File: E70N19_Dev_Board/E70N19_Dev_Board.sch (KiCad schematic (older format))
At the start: 71 parts, among them J1 USB_OTG, J2 Battery 1x2, J3 JTAGSEL_JUMPER 1x3, J4 UART_PROG 1x2, J5 ERASE_JUMPER 1x3, J6 ARM-Cortex-Debug-10, J7 CAN 1x2, J8 Conn_02x15_Counter_Clockwise, J9 Conn_02x15_Counter_Clockwise, SW1 NRST_BUTTON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

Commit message: Brad's micro OTG connector
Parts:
- removed J1: USB_OTG, Connect:USB_Micro-B, symbol USB_OTG-RESCUE-E70N19_Dev_Board
- added J?: USB_microB_2040002-1, symbol USB_microB_2040002-1
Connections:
- wire segments 231 -> 238
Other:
- moved on the sheet: C1, C10, C11, C12, C13, C14, C15, C16, C17, C18, C19, C2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

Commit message: More footprints
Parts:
- removed Y1: Crystal_GND23_Small, symbol Crystal_GND23_Small
- added Y1: Crystal_Small, eclectronics:ECS-.327-12.5-34B-TR, symbol Crystal_Small
- FP1: footprint (none) -> eclectronics:BM71BLES1FC2
- J1: renamed from J?; footprint (none) -> eclectronics:USB_microB_2040002-1
- J3, J5: footprint (none) -> Pin_Headers:Pin_Header_Straight_1x03_Pitch2.54mm
- J4, J7, SW1: footprint (none) -> Pin_Headers:Pin_Header_Straight_1x02_Pitch2.54mm
- J6: footprint (none) -> Pin_Headers:Pin_Header_Straight_2x05_Pitch2.54mm
- J8, J9: footprint (none) -> Pin_Headers:Pin_Header_Straight_2x15_Pitch2.54mm
- L1, L2, R1, R10, R11, R12, R13, R14, R15, R2, R3, R4, R5, R6, R7, R8, R9: footprint (none) -> Resistors_SMD:R_0603
- U1: footprint (none) -> TO_SOT_Packages_SMD:SOT-23-5
- U2: footprint (none) -> Housings_SSOP:TSSOP-8_4.4x3mm_Pitch0.65mm
- U4: footprint (none) -> Housings_QFP:LQFP-100_14x14mm_Pitch0.5mm
- U5: footprint (none) -> TO_SOT_Packages_SMD:SOT-23
- U6: footprint (none) -> Housings_SOIC:SOIC-8_3.9x4.9mm_Pitch1.27mm
- Y2: footprint (none) -> Crystals:Crystal_SMD_SeikoEpson_FA238-4pin_3.2x2.5mm
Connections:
- net at C31.1, U4.24 (PA7/XIN32): now also Y1.1
- net at C32.1, U4.25 (PA8/XOUT32): now also Y1.2
- no-connect marks 22 -> 20

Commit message: Finishing PCB component placement
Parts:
- SW1: footprint Pin_Headers:Pin_Header_Straight_1x02_Pitch2.54mm -> eclectronics:PTS820_J15M_SMTR_LFS
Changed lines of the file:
@@
 F 0 "SW1" H 6075 6100 50  0000 L CNN
 F 1 "NRST_BUTTON" H 6025 5940 50  0000 C CNN
-F 2 "Pin_Headers:Pin_Header_Straight_1x02_Pitch2.54mm" H 6025 6200 50  0001 C CNN
-F 3 "" H 6025 6200 50  0001 C CNN
+F 2 "eclectronics:PTS820_J15M_SMTR_LFS" H 6025 6200 50  0001 C CNN
+F 3 " CKN10506CT-ND " H 6025 6200 50  0001 C CNN
 F 4 "Value" H 6025 6000 60  0001 C CNN "Fieldname"
 	1    6025 6000

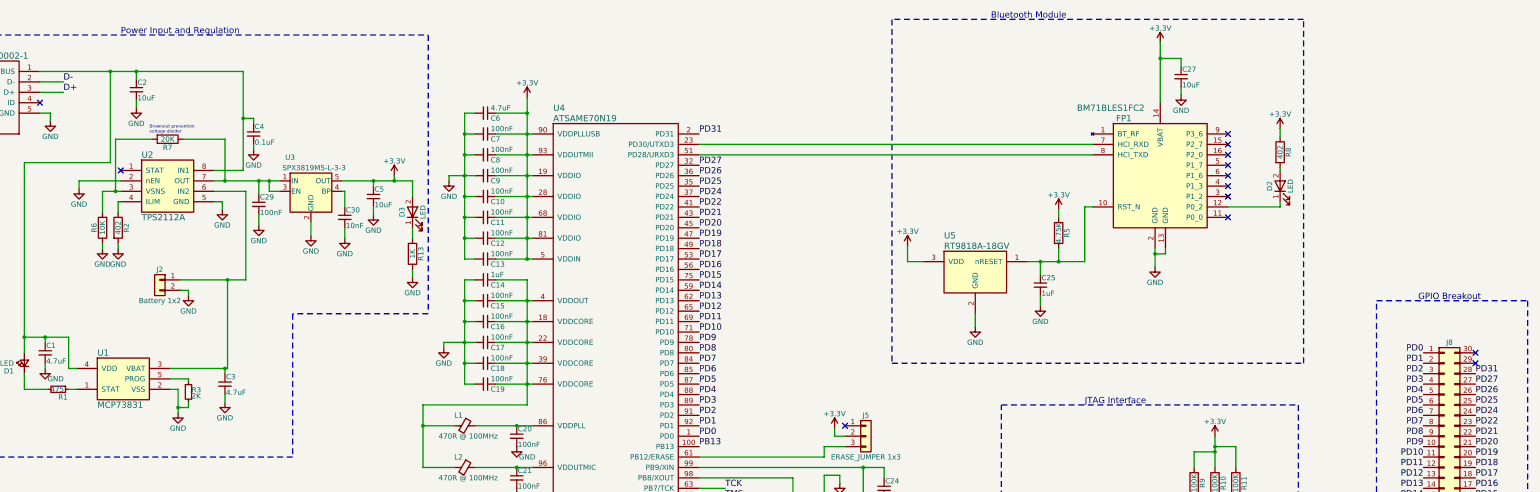
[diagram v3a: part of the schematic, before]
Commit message: Added debug LEDs
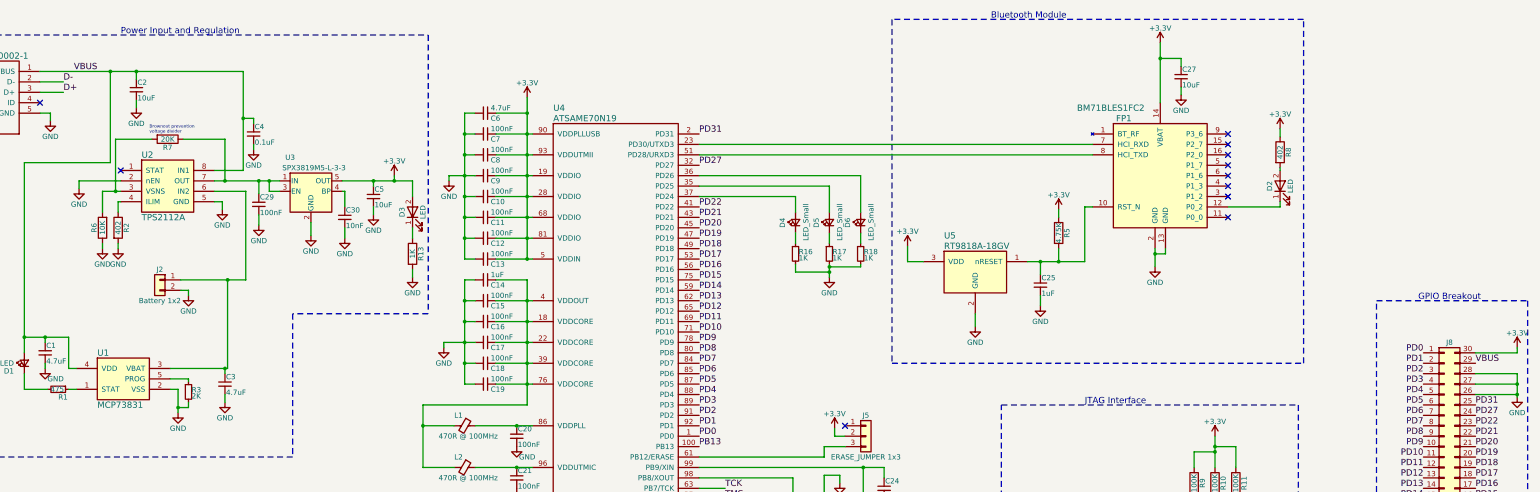
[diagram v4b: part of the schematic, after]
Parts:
- added D4, D5, D6: LED_Small, LEDs:LED_0805, symbol LED_Small
- added R16, R17, R18: 1K, Resistors_SMD:R_0603, symbol R_Small
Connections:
- net +3V3: now also J8.30 (Pin_30)
- net GND: now also J8.26 (Pin_26), J8.27 (Pin_27), J8.28 (Pin_28), R16.2, R17.2, R18.2
- net PD27: now also J8.24 (Pin_24); no longer J8.27 (Pin_27)
- net PD31: now also J8.25 (Pin_25); no longer J8.28 (Pin_28)
- net VBUS: now reaches J8.29 (Pin_29)
- net VBUS: now also C1.1, C2.1, C4.1, D1.2 (A), J1.1 (VBUS), U1.4 (VDD), U2.8 (IN1)
- net PD24: no longer names the net of U4.37 (PD24)
- net PD24: now also D4.2 (A); no longer J8.24 (Pin_24)
- net PD25: no longer names the net of U4.35 (PD25)
- net PD25: now also D5.2 (A); no longer J8.25 (Pin_25)
- net PD26: no longer names the net of U4.36 (PD26)
- net PD26: now also D6.2 (A); no longer J8.26 (Pin_26)
- new net: D4.1 (K), R16.1
- new net: D5.1 (K), R17.1
- new net: D6.1 (K), R18.1
- no-connect marks 20 -> 18

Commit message: Initial routing
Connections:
- net D_N: now reaches R14.1, U4.94 (HSDM)
- net D_P: now reaches R15.1, U4.95 (HSDP)
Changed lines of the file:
@@
 Wire Wire Line
 	16225 3850 16225 3800
+Text Label 6725 6500 0    60   ~ 0
+D_N
+Text Label 6725 6600 0    60   ~ 0
+D_P
 $EndSCHEMATC
